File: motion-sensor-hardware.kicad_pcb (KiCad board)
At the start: 2 copper layers, 76.2 x 50.8 mm, 59 parts, among them J1 MX128-2.54-02P, J2 TYPE-C 16PIN 2MD(073), J3 PZ254V-11-03P, J4 MX128-2.54-04P, Q1 AO3401A, SW1 TS-1088-AR02016, SW2 TS-1088-AR02016, U1 USBLC6-2SC6, U2 ASSR-1218, U3 LD2410C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

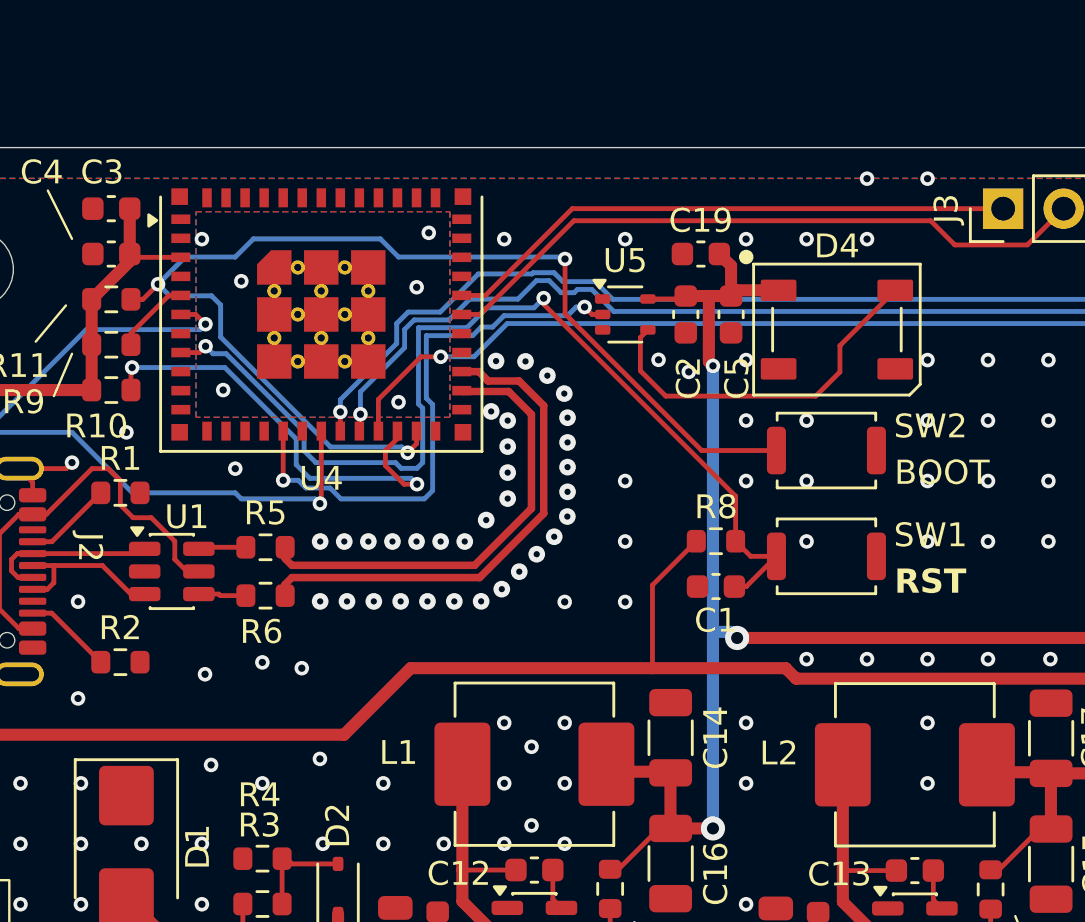
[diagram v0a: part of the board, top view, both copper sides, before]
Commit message: Got 3D export working
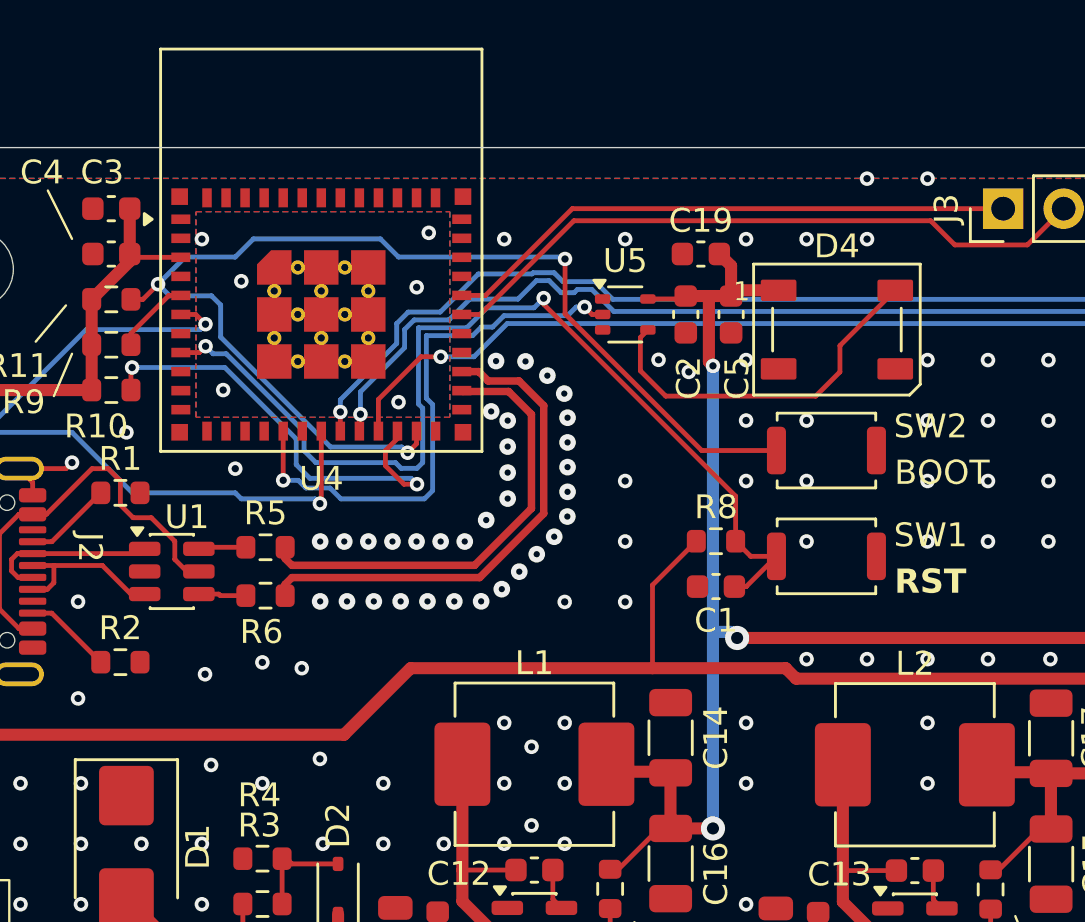
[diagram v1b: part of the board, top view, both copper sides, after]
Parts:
- L1, L2: footprint Inductor_SMD:L_Changjiang_FXL0630 -> !Inductors:L_Changjiang_FXL0630
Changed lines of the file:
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@@
 			(layer "F.SilkS")
 		)
-		(fp_circle
-			(center -3.81 -3.048)
-			(end -3.556 -3.048)
-			(stroke
-				(width 0.1)
-				(type solid)
-			)
-			(fill yes)
-			(layer "F.SilkS")
-		)
 		(fp_line
 			(start -3.45 -2.75)
@@
 			(layer "F.Fab")
 		)
+		(fp_text user "1"
+			(at -4 -1.6 0)
+			(unlocked yes)
+			(layer "F.SilkS")
+			(effects
+				(font
+					(size 0.8 0.8)
+					(thickness 0.15)
+				)
+			)
+		)
 		(fp_text user "${REFERENCE}"
 			(at 0 0 0)
@@
 		)
 		(embedded_fonts no)
-		(model "${KIPRJMOD}/libraries/HLK-LD2410C/3d/HLK-LD2410C.step"
+		(model "${KILIB_DIR}/3dmodels/LD2410C mmWave Sensor.step"
 			(offset
-				(xyz -157.5 -42.7 5)
+				(xyz -6 -14.5 2.2)
 			)
 			(scale
@@
 			(drill 3.2)
 			(layers "*.Cu" "*.Mask")
-			(clearance 1.6)
 		)
 		(embedded_fonts no)
@@
 		)
 	)
-	(footprint "Inductor_SMD:L_Changjiang_FXL0630"
+	(footprint "!Inductors:L_Changjiang_FXL0630"
 		(layer "F.Cu")
 		(at 103.5675 102.5775)
@@
 		(tags "power shielded cjiang fxl")
 		(property "Reference" "L1"
-			(at -5.7075 -0.4775 0)
+			(at 0 -4.25 0)
 			(layer "F.SilkS")
 			(effects
@@
 		)
 		(embedded_fonts no)
-		(model "${KICAD9_3DMODEL_DIR}/Inductor_SMD.3dshapes/L_Changjiang_FXL0630.step"
+		(model "${KILIB_DIR}/3dmodels/ASPI-0630LR.step"
 			(offset
 				(xyz 0 0 0)
@@
 		)
 	)
-	(footprint "Inductor_SMD:L_Changjiang_FXL0630"
+	(footprint "!Inductors:L_Changjiang_FXL0630"
 		(layer "F.Cu")
 		(at 119.549656 102.6)
@@
 		(tags "power shielded cjiang fxl")
 		(property "Reference" "L2"
-			(at -5.7075 -0.4775 0)
+			(at 0 -4.25 0)
 			(layer "F.SilkS")
 			(effects
@@
 		)
 		(embedded_fonts no)
-		(model "${KICAD9_3DMODEL_DIR}/Inductor_SMD.3dshapes/L_Changjiang_FXL0630.step"
+		(model "${KILIB_DIR}/3dmodels/ASPI-0630LR.step"
 			(offset
 				(xyz 0 0 0)
@@
 			)
 		)
+		(property "JLCPCB" "C2838502"
+			(at 0 0 0)
+			(unlocked yes)
+			(layer "F.Fab")
+			(hide yes)
+			(effects
+				(font
+					(size 1 1)
+					(thickness 0.15)
+				)
+			)
+		)
+		(property "JLPCB" ""
+			(at 0 0 0)
+			(unlocked yes)
+			(layer "F.Fab")
+			(hide yes)
+			(effects
+				(font
+					(size 1 1)
+					(thickness 0.15)
+				)
+			)
+		)
 		(property "JLCPCB PN" "C2838502"
 			(at 0 0 0)
@@
 		(attr smd)
 		(fp_line
+			(start -6.75 -11.15)
+			(end 6.75 -11.15)
+			(stroke
+				(width 0.12)
+				(type solid)
+			)
+			(layer "F.SilkS")
+		)
+		(fp_line
 			(start -6.75 5.75)
-			(end -6.75 -4.9375)
+			(end -6.75 -11.15)
 			(stroke
 				(width 0.12)
@@
 		)
 		(fp_line
-			(start 6.75 -4.9375)
+			(start 6.75 -11.15)
 			(end 6.75 5.75)
 			(stroke
@@
 		(fp_poly
 			(pts
-				(xy -6.9125 -3.95) (xy -7.2485 -3.71) (xy -7.2485 -4.19) (xy -6.9125 -3.95)
+				(xy -7.1 -4) (xy -7.436 -3.76) (xy -7.436 -4.24) (xy -7.1 -4)
 			)
 			(stroke
@@
 		)
 		(embedded_fonts no)
-		(model "${KICAD9_3DMODEL_DIR}/RF_Module.3dshapes/ESP32-C6-MINI-1.step"
+		(model "${KICAD_USER_3DMODEL_DIR}/ESP32-C3-MINI-1-N4.step"
 			(offset
 				(xyz 0 0 0)
@@
 			)
 			(rotate
-				(xyz 0 0 0)
+				(xyz -90 -0 -0)
 			)
 		)
@@
 			(drill 3.2)
 			(layers "*.Cu" "*.Mask")
-			(clearance 1.6)
 		)
 		(embedded_fonts no)
@@
 		)
 		(embedded_fonts no)
-		(model "${MY_3DMODEL_DIR}/1725656.step"
+		(model "${KILIB_DIR}/3dmodels/1725656.step"
 			(offset
 				(xyz 4 3.1 0)
@@
 		)
 		(embedded_fonts no)
-		(model "${MY_3DMODEL_DIR}/pxc_1725672_06_02_MPT-0-5-4-2-54_3D.stp"
+		(model "${KILIB_DIR}/3dmodels/pxc_1725672_06_02_MPT-0-5-4-2-54_3D.stp"
 			(offset
 				(xyz 9.15 3.1 0)
@@
 			(drill 3.2)
 			(layers "*.Cu" "*.Mask")
-			(clearance 1.6)
 		)
 		(embedded_fonts no)
@@
 			(drill 3.2)
 			(layers "*.Cu" "*.Mask")
-			(clearance 1.6)
 		)
 		(embedded_fonts no)
@@
 			(keep_text_aligned yes)
 		)
-		(gr_text "3000"
+		(gr_text "76.2"
 			(at 113.1 133.335 0)
 			(layer "Dwgs.User")
@@
 			(keep_text_aligned yes)
 		)
-		(gr_text "2000"
+		(gr_text "50.8"
 			(at 68.77 102.1 90)
 			(layer "Dwgs.User")

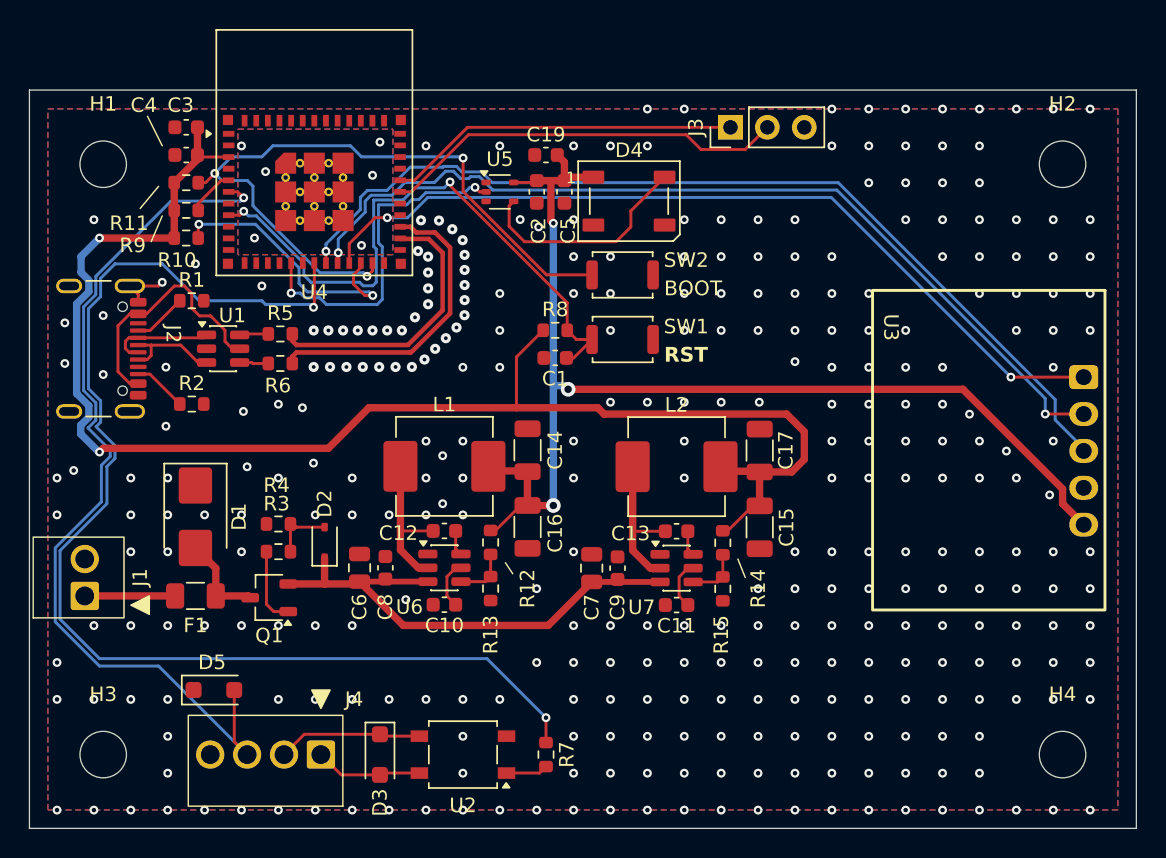
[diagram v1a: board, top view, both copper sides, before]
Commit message: Fixed screw term pin 1 issue
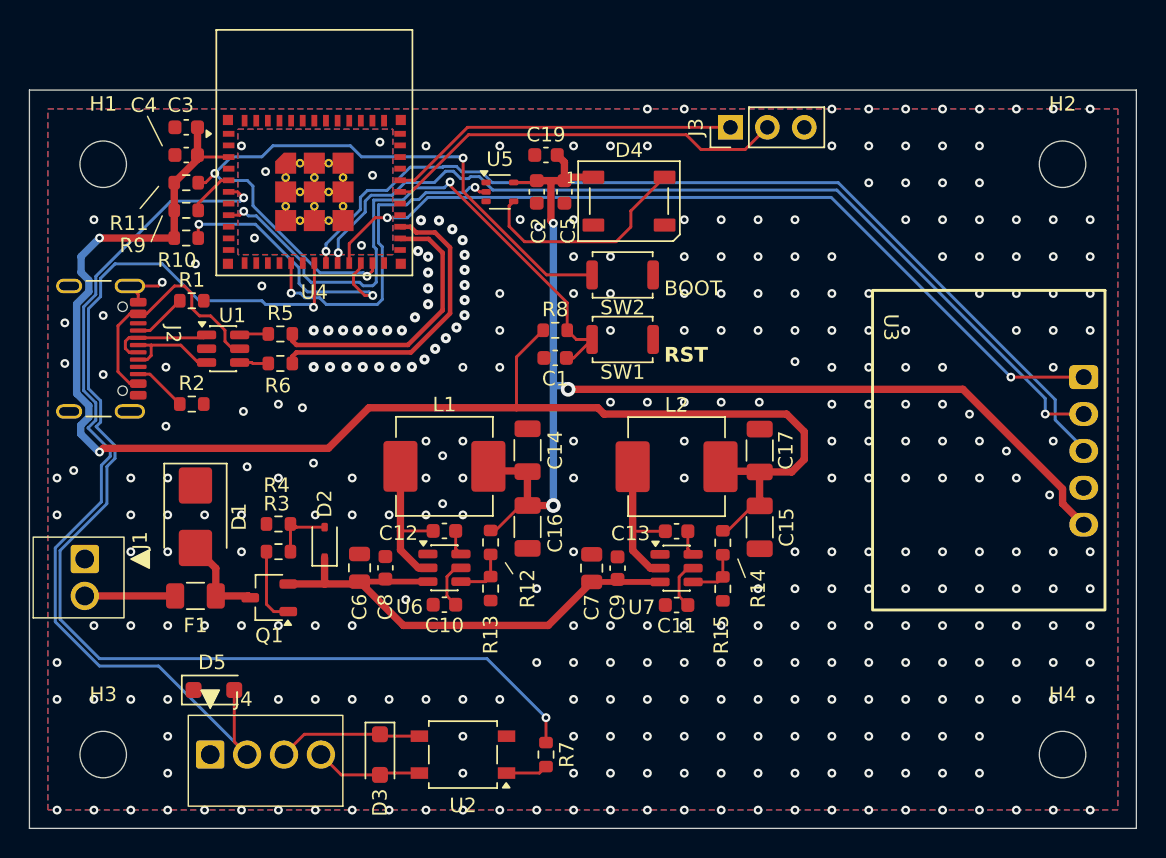
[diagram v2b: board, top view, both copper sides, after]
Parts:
- SW1, SW2: footprint Button_Switch_SMD:SW_Push_SPST_NO_Alps_SKRK -> !Switches:SW_TS-1088-xx020xx_XUNPU
- moved J4 7.62 mm to (87.4, 122.4)
- moved J1 2.54 mm to (78.8, 109.0)
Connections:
- J1 pad 1: /VRAW -> GND
- J1 pad 2: GND -> /VRAW
- J4 pad 1: /CTL_SW1 -> GND
- J4 pad 2: /CTL_SW2 -> /STAT_SW
- J4 pad 3: /STAT_SW -> /CTL_SW2
- J4 pad 4: GND -> /CTL_SW1
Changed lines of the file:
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@@
 		)
 	)
-	(footprint "Button_Switch_SMD:SW_Push_SPST_NO_Alps_SKRK"
+	(footprint "!Switches:SW_TS-1088-xx020xx_XUNPU"
 		(layer "F.Cu")
 		(at 115.835 89.4 180)
@@
 		(tags "SMD SMT button")
 		(property "Reference" "SW2"
-			(at -4.377 1.016 0)
+			(at 0 -2.25 180)
 			(layer "F.SilkS")
 			(effects
@@
 		)
 		(property "Value" "TS-1088-AR02016"
-			(at 0 2.5 0)
+			(at 0 2.5 180)
 			(layer "F.Fab")
 			(effects
@@
 		)
 		(fp_text user "${REFERENCE}"
-			(at 0 0 0)
+			(at 0 0 180)
 			(layer "F.Fab")
 			(effects
@@
 		)
 		(embedded_fonts no)
-		(model "${KICAD9_3DMODEL_DIR}/Button_Switch_SMD.3dshapes/SW_Push_SPST_NO_Alps_SKRK.step"
+		(model "${KILIB_DIR}/3dmodels/SW_TS-1088-xx020xx.step"
 			(offset
 				(xyz 0 0 0)
@@
 		)
 		(embedded_fonts no)
-		(model "${KICAD_USER_3DMODEL_DIR}/ESP32-C3-MINI-1-N4.step"
+		(model "${KILIB_DIR}/3dmodels/ESP32-C3-MINI-1-N4.step"
 			(offset
 				(xyz 0 0 0)
@@
 	(footprint "!Connectors:MX128-2.54-02P"
 		(layer "F.Cu")
-		(at 78.81 111.498 90)
+		(at 78.81 108.958 90)
 		(property "Reference" "J1"
 			(at 1.27 3.81 90)
@@
 		(attr through_hole)
 		(fp_rect
-			(start -1.51 -3.55)
-			(end 4.05 2.7)
+			(start -4.05 -3.55)
+			(end 1.51 2.7)
 			(stroke
 				(width 0.1)
@@
 		(fp_poly
 			(pts
-				(xy -0.635 3.175) (xy -1.27 4.445) (xy 0 4.445)
+				(xy 0 3.175) (xy -0.635 4.445) (xy 0.635 4.445)
 			)
 			(stroke
@@
 		(fp_poly
 			(pts
-				(xy 1.21 -3.75) (xy -1.29 -6.25) (xy -0.29 -6.25) (xy -0.29 -9.75) (xy 2.71 -9.75) (xy 2.71 -6.25)
-				(xy 3.71 -6.25)
+				(xy -1.33 -3.75) (xy -3.83 -6.25) (xy -2.83 -6.25) (xy -2.83 -9.75) (xy 0.17 -9.75) (xy 0.17 -6.25)
+				(xy 1.17 -6.25)
 			)
 			(stroke
@@
 		)
 		(fp_rect
-			(start -1.76 -3.8)
-			(end 4.3 2.95)
+			(start -4.3 -3.8)
+			(end 1.76 2.95)
 			(stroke
 				(width 0.05)
@@
 		)
 		(fp_rect
-			(start -1.51 -3.55)
-			(end 4.05 2.7)
+			(start -4.05 -3.55)
+			(end 1.51 2.7)
 			(stroke
 				(width 0.1)
@@
 			(remove_unused_layers no)
 			(roundrect_rratio 0.1)
-			(net 52 "/VRAW")
+			(net 4 "GND")
 			(pinfunction "Pin_1")
 			(pintype "passive")
@@
 		)
 		(pad "2" thru_hole circle
-			(at 2.54 0 90)
+			(at -2.54 0 90)
 			(size 1.95 1.95)
 			(drill 1.3)
 			(layers "*.Cu" "*.Mask")
 			(remove_unused_layers no)
-			(net 4 "GND")
+			(net 52 "/VRAW")
 			(pinfunction "Pin_2")
 			(pintype "passive")
@@
 		(model "${KILIB_DIR}/3dmodels/1725656.step"
 			(offset
-				(xyz 4 3.1 0)
+				(xyz 1.46 3.1 0)
 			)
 			(scale
@@
 	(footprint "!Connectors:MX128-2.54-04P"
 		(layer "F.Cu")
-		(at 95.066 122.42 180)
+		(at 87.446 122.42 180)
 		(property "Reference" "J4"
 			(at -2.286 3.81 0)
@@
 		(attr through_hole)
 		(fp_rect
-			(start -1.51 -3.55)
-			(end 9.13 2.7)
+			(start -9.13 -3.55)
+			(end 1.51 2.7)
 			(stroke
 				(width 0.1)
@@
 		)
 		(fp_rect
-			(start -1.76 -3.8)
-			(end 9.38 2.95)
+			(start -9.38 -3.8)
+			(end 1.76 2.95)
 			(stroke
 				(width 0.05)
@@
 		)
 		(fp_rect
-			(start -1.51 -3.55)
-			(end 9.13 2.7)
+			(start -9.13 -3.55)
+			(end 1.51 2.7)
 			(stroke
 				(width 0.1)
@@
 		(fp_poly
 			(pts
-				(xy 3.75 -3.75) (xy 1.25 -6.25) (xy 2.25 -6.25) (xy 2.25 -9.75) (xy 5.25 -9.75) (xy 5.25 -6.25)
-				(xy 6.25 -6.25)
+				(xy -3.87 -3.75) (xy -6.37 -6.25) (xy -5.37 -6.25) (xy -5.37 -9.75) (xy -2.37 -9.75) (xy -2.37 -6.25)
+				(xy -1.37 -6.25)
 			)
 			(stroke
@@
 			(remove_unused_layers no)
 			(roundrect_rratio 0.1)
-			(net 47 "/CTL_SW1")
+			(net 4 "GND")
 			(pinfunction "Pin_1")
 			(pintype "passive")
@@
 		)
 		(pad "2" thru_hole circle
-			(at 2.54 0 180)
+			(at -2.54 0 180)
 			(size 1.95 1.95)
 			(drill 1.3)
 			(layers "*.Cu" "*.Mask")
 			(remove_unused_layers no)
-			(net 46 "/CTL_SW2")
+			(net 48 "/STAT_SW")
 			(pinfunction "Pin_2")
 			(pintype "passive")
 		)
 		(pad "3" thru_hole circle
-			(at 5.08 0 180)
+			(at -5.08 0 180)
 			(size 1.95 1.95)
 			(drill 1.3)
 			(layers "*.Cu" "*.Mask")
 			(remove_unused_layers no)
-			(net 48 "/STAT_SW")
+			(net 46 "/CTL_SW2")
 			(pinfunction "Pin_3")
 			(pintype "passive")
 		)
 		(pad "4" thru_hole circle
-			(at 7.62 0 180)
+			(at -7.62 0 180)
 			(size 1.95 1.95)
 			(drill 1.3)
 			(layers "*.Cu" "*.Mask")
 			(remove_unused_layers no)
-			(net 4 "GND")
+			(net 47 "/CTL_SW1")
 			(pinfunction "Pin_4")
 			(pintype "passive")
@@
 		(model "${KILIB_DIR}/3dmodels/pxc_1725672_06_02_MPT-0-5-4-2-54_3D.stp"
 			(offset
-				(xyz 9.15 3.1 0)
+				(xyz 1.53 3.1 0)
 			)
 			(scale
@@
 		)
 	)
-	(footprint "Button_Switch_SMD:SW_Push_SPST_NO_Alps_SKRK"
+	(footprint "!Switches:SW_TS-1088-xx020xx_XUNPU"
 		(layer "F.Cu")
 		(at 115.835 93.845 180)
@@
 		(tags "SMD SMT button")
 		(property "Reference" "SW1"
-			(at -4.377 0.889 0)
+			(at 0 -2.25 180)
 			(layer "F.SilkS")
 			(effects
@@
 		)
 		(property "Value" "TS-1088-AR02016"
-			(at 0 2.5 0)
+			(at 0 2.5 180)
 			(layer "F.Fab")
 			(effects
@@
 		)
 		(fp_text user "${REFERENCE}"
-			(at 0 0 0)
+			(at 0 0 180)
 			(layer "F.Fab")
 			(effects
@@
 		)
 		(embedded_fonts no)
-		(model "${KICAD9_3DMODEL_DIR}/Button_Switch_SMD.3dshapes/SW_Push_SPST_NO_Alps_SKRK.step"
+		(model "${KILIB_DIR}/3dmodels/SW_TS-1088-xx020xx.step"
 			(offset
 				(xyz 0 0 0)
@@
 			(keep_text_aligned yes)
 		)
-		(gr_text "76.2"
+		(gr_text "3000"
 			(at 113.1 133.335 0)
 			(layer "Dwgs.User")
@@
 			(keep_text_aligned yes)
 		)
-		(gr_text "50.8"
+		(gr_text "2000"
 			(at 68.77 102.1 90)
 			(layer "Dwgs.User")
